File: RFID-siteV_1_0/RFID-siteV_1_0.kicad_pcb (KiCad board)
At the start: 2 copper layers, 40 parts, among them J1 USB_C_Receptacle_USB2.0, J2 Conn_01x05_Male, J3 Conn_01x05_Female, Q1 MMBT3904, SW1 SW_Push, U1 XC6206P332MR, U2 STM32L053R8Tx, U3 E22-400T22S

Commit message: update
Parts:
- added H1: MountingHole, MountingHole:MountingHole_2.5mm, F.Cu at (78.2, 106.0)
- added H2: MountingHole, MountingHole:MountingHole_2.5mm, F.Cu at (78.2, 131.9)
- added H3: MountingHole, MountingHole:MountingHole_2.5mm, F.Cu at (78.2, 161.9)
- added H4: MountingHole, MountingHole:MountingHole_2.5mm, F.Cu at (116.2, 161.9)
- added H5: MountingHole, MountingHole:MountingHole_2.5mm, F.Cu at (116.2, 131.9)
- added H6: MountingHole, MountingHole:MountingHole_2.5mm, F.Cu at (116.2, 106.0)
- added J4: Conn_01x03_Male, Connector_PinHeader_2.54mm:PinHeader_1x03_P2.54mm_Vertical, F.Cu at (92.3, 141.4)
- JP2, JP3, JP4, JP5: moved to B.Cu
- moved R2 170.4 mm to (90.1, 169.7), turned to 90 degrees
- moved D2 166.0 mm to (72.9, 160.3), turned to 90 degrees
- moved C6 163.0 mm to (87.7, 151.2), turned to 90 degrees
- moved R3 161.6 mm to (85.8, 173.4), turned to 180 degrees
- moved D4 153.4 mm to (72.9, 152.6), turned to 90 degrees
- moved C5 150.9 mm to (93.6, 146.2)
- moved R13 148.7 mm to (93.9, 138.6)
- moved J1 146.9 mm to (97.2, 170.8)
- moved C2 145.8 mm to (83.6, 169.2), turned to -90 degrees
- moved R10 145.4 mm to (100.0, 119.4)
- moved C3 145.0 mm to (100.4, 146.1)
- moved Q1 144.5 mm to (86.6, 143.4), turned to 180 degrees
- moved R4 142.7 mm to (86.8, 146.2)
- moved R7 142.3 mm to (76.9, 155.0)
- moved R5 142.2 mm to (76.9, 157.0)
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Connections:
- U2 pad 46: unconnected-(U2-Pad46) -> /SWDIO
- U2 pad 49: unconnected-(U2-Pad49) -> /SWCLK
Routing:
- net /LoRa_RXD_: track 0.00 -> 19.3 mm
- net /LoRa_TXD_: track 0.00 -> 18.8 mm
- net /ANT: track 0.00 -> 7.24 mm
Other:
- board outline added: 52 x 95 mm

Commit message: update
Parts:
- added C8: 0.1uF, Capacitor_SMD:C_0805_2012Metric, F.Cu at (100.0, 161.9)
- moved J4 10.1 mm to (121.1, 152.0), turned to 180 degrees
- moved R11 9.59 mm to (107.9, 139.8), turned to 0 degrees
- moved D4 7.67 mm to (72.8, 160.3)
- moved D2 7.37 mm to (72.8, 152.9)
- moved C9 7.32 mm to (107.9, 141.9), turned to 180 degrees
- moved R5 6.92 mm to (79.7, 150.7)
- moved SW1 4.95 mm to (114.3, 143.4), turned to 180 degrees
- moved R7 3.59 mm to (79.7, 152.7)
- moved R8 3.25 mm to (79.7, 154.8)
- moved BZ1 2.42 mm to (78.8, 141.6)
- moved J2 1.75 mm to (119.1, 112.9)
- moved R2 0.84 mm to (90.1, 168.9)
- moved R6 0.66 mm to (86.3, 139.8)
- moved Q1 0.66 mm to (87.3, 143.3)
- moved R4 0.66 mm to (87.5, 146.1)
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- renumbered C8 to C9, J4 to J3, J3 to J4, JP2 to JP1, JP3 to JP2, JP4 to JP3, JP5 to JP4
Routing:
- net +3V3: track 0.00 -> 290.2 mm, vias 0 -> 2
- net +5V: track 0.00 -> 120.3 mm, vias 0 -> 2
- net /L53R8_UART1_TX: track 0.00 -> 72.8 mm, vias 0 -> 1
- net /L53R8_UART1_RX: track 0.00 -> 68.5 mm, vias 0 -> 1
- net /LoRa_AUX: track 0.00 -> 54.7 mm, vias 0 -> 2
- net /BOOT0: track 0.00 -> 32.3 mm, vias 0 -> 2
- net /NRST: track 0.00 -> 30.7 mm, vias 0 -> 2
- net /SWDIO: track 0.00 -> 29.3 mm, vias 0 -> 2
- net GND: track 0.00 -> 27.1 mm, vias 0 -> 14
- net /SWCLK: track 0.00 -> 25.2 mm, vias 0 -> 2
- net /PB0: track 0.00 -> 19.6 mm
- net Net-(F1-Pad2): track 0.00 -> 19.5 mm, vias 0 -> 2
- net /PB2: track 0.00 -> 19.4 mm
- net /PB1: track 0.00 -> 18.2 mm
- net /buz: track 0.00 -> 17.1 mm, vias 0 -> 2
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- added copper zone on B.Cu, net GND
- added copper zone on F.Cu, net GND
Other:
- board text added: "JP1:M0 JP2:M1 JP3:LoRa RX JP4:Lora TX"

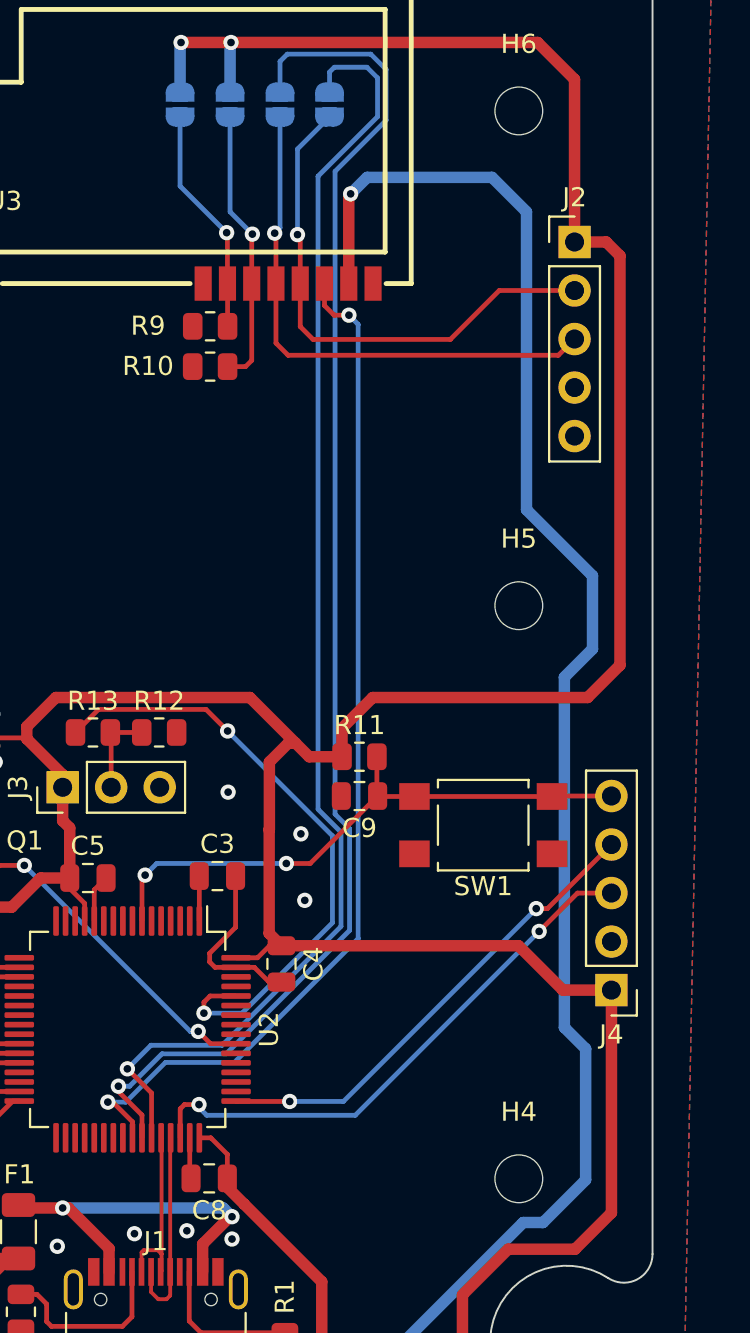
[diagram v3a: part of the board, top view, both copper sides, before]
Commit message: Update RFID-siteV_1_0.kicad_pcb
V1.ST-LINK 腳位上下顛倒，接腳不便使用。
V2.缺少模式(加符號&不加符號)選擇接點。
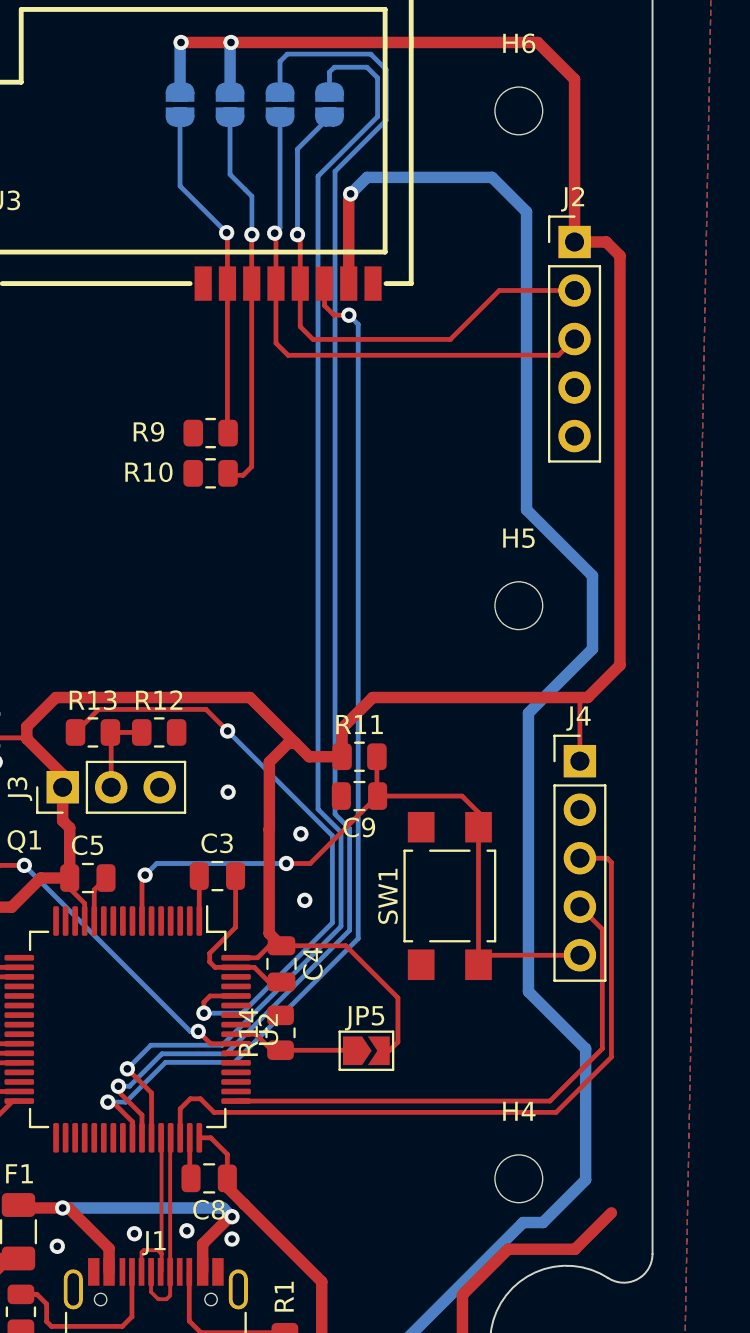
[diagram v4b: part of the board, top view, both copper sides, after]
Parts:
- added JP5: SolderJumper_2_Open, Jumper:SolderJumper-2_P1.3mm_Open_TrianglePad1.0x1.5mm, F.Cu at (108.2, 155.2)
- added R14: 1k, Resistor_SMD:R_0805_2012Metric, F.Cu at (103.7, 154.3)
- moved J4 12.1 mm to (119.4, 140.1), turned to 0 degrees
- moved R10 5.59 mm to (100.1, 125.0)
- moved R9 5.59 mm to (100.1, 122.9)
- moved SW1 4.10 mm to (112.6, 147.1), turned to 90 degrees
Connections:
- U2 pad 56: unconnected-(U2-Pad56) -> /mod_sel
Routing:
- net +3V3: track 290.2 -> 274.3 mm
- net /SWDIO: track 29.3 -> 37.7 mm, vias 2 -> 0
- net /NRST: track 30.7 -> 37.5 mm
- net /mod_sel: track 0.00 -> 6.46 mm
- net /M1: track 14.6 -> 20.3 mm
- net /M0: track 12.0 -> 17.6 mm
- net /SWCLK: track 25.2 -> 28.2 mm, vias 2 -> 0
- net +5V: track 120.3 -> 121.9 mm
